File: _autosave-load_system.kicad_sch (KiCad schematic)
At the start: 1 part

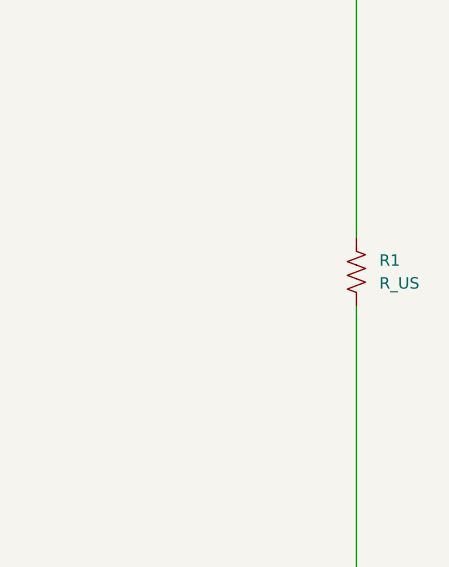
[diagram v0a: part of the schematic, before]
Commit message: feat:added resistor as a load and added demo connections to minimize ERC errors(2)
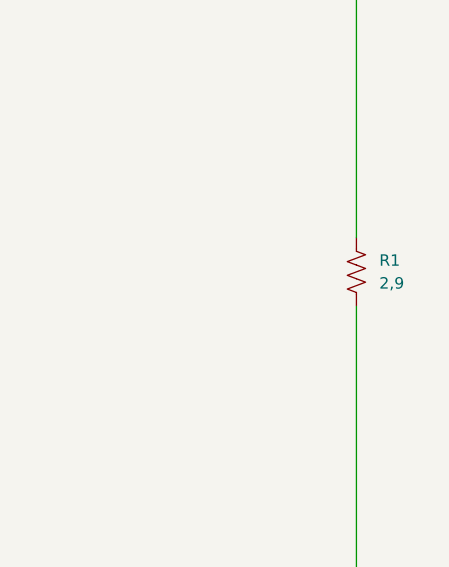
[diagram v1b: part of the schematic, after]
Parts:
- R1: value R_US -> 2,9
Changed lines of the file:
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@@
 			)
 		)
-		(property "Value" "R_US"
+		(property "Value" "2,9"
 			(at 111.76 99.0599 0)
 			(effects
